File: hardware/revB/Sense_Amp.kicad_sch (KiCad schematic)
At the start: 3 parts, among them U17 INA240A3EDRQ1

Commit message: working revB
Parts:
- renumbered C52 to C36, C53 to C37, U17 to U15
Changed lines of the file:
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@@
   (symbol (lib_id "Device:C") (at 121.92 71.12 0) (unit 1)
     (in_bom yes) (on_board yes) (dnp no) (fields_autoplaced)
-    (property "Reference" "C52" (at 124.841 70.2115 0)
+    (property "Reference" "C36" (at 124.841 70.2115 0)
       (effects (font (size 1.27 1.27)) (justify left))
     )
@@
       (project "FP Interface Card"
         (path "/dc2801a1-d539-4721-b31f-fe196b9f13df/66fbc293-b490-4097-aa2e-a081509eef04/b12d78bf-aa15-467a-b4b1-b3adfb073398"
-          (reference "C52") (unit 1)
+          (reference "C36") (unit 1)
         )
         (path "/dc2801a1-d539-4721-b31f-fe196b9f13df/66fbc293-b490-4097-aa2e-a081509eef04/c0544bb0-133b-49a1-b8f9-e77504492c11"
-          (reference "C54") (unit 1)
+          (reference "C38") (unit 1)
         )
         (path "/dc2801a1-d539-4721-b31f-fe196b9f13df/66fbc293-b490-4097-aa2e-a081509eef04/055667d1-a090-4d44-b096-566c0357f041"
-          (reference "C59") (unit 1)
+          (reference "C41") (unit 1)
         )
       )
@@
   (symbol (lib_id "power:GND") (at 144.78 109.22 0) (unit 1)
     (in_bom yes) (on_board yes) (dnp no) (fields_autoplaced)
-    (property "Reference" "#PWR049" (at 144.78 115.57 0)
+    (property "Reference" "#PWR079" (at 144.78 115.57 0)
       (effects (font (size 1.27 1.27)) hide)
     )
@@
       (project "FP Interface Card"
         (path "/dc2801a1-d539-4721-b31f-fe196b9f13df/66fbc293-b490-4097-aa2e-a081509eef04/b12d78bf-aa15-467a-b4b1-b3adfb073398"
-          (reference "#PWR049") (unit 1)
+          (reference "#PWR079") (unit 1)
         )
         (path "/dc2801a1-d539-4721-b31f-fe196b9f13df/66fbc293-b490-4097-aa2e-a081509eef04/c0544bb0-133b-49a1-b8f9-e77504492c11"
-          (reference "#PWR051") (unit 1)
+          (reference "#PWR081") (unit 1)
         )
         (path "/dc2801a1-d539-4721-b31f-fe196b9f13df/66fbc293-b490-4097-aa2e-a081509eef04/055667d1-a090-4d44-b096-566c0357f041"
-          (reference "#PWR058") (unit 1)
+          (reference "#PWR087") (unit 1)
         )
       )
@@
   (symbol (lib_id "Device:C") (at 130.81 71.12 0) (unit 1)
     (in_bom yes) (on_board yes) (dnp no) (fields_autoplaced)
-    (property "Reference" "C53" (at 133.731 70.2115 0)
+    (property "Reference" "C37" (at 133.731 70.2115 0)
       (effects (font (size 1.27 1.27)) (justify left))
     )
@@
       (project "FP Interface Card"
         (path "/dc2801a1-d539-4721-b31f-fe196b9f13df/66fbc293-b490-4097-aa2e-a081509eef04/b12d78bf-aa15-467a-b4b1-b3adfb073398"
-          (reference "C53") (unit 1)
+          (reference "C37") (unit 1)
         )
         (path "/dc2801a1-d539-4721-b31f-fe196b9f13df/66fbc293-b490-4097-aa2e-a081509eef04/c0544bb0-133b-49a1-b8f9-e77504492c11"
-          (reference "C55") (unit 1)
+          (reference "C39") (unit 1)
         )
         (path "/dc2801a1-d539-4721-b31f-fe196b9f13df/66fbc293-b490-4097-aa2e-a081509eef04/055667d1-a090-4d44-b096-566c0357f041"
-          (reference "C60") (unit 1)
+          (reference "C42") (unit 1)
         )
       )
@@
   (symbol (lib_id "FP-Interface-Card:INA240AxxD") (at 147.32 97.79 0) (unit 1)
     (in_bom yes) (on_board yes) (dnp no)
-    (property "Reference" "U17" (at 152.4 91.44 0)
+    (property "Reference" "U15" (at 152.4 91.44 0)
       (effects (font (size 1.27 1.27)))
     )
@@
       (project "FP Interface Card"
         (path "/dc2801a1-d539-4721-b31f-fe196b9f13df/66fbc293-b490-4097-aa2e-a081509eef04/b12d78bf-aa15-467a-b4b1-b3adfb073398"
-          (reference "U17") (unit 1)
+          (reference "U15") (unit 1)
         )
         (path "/dc2801a1-d539-4721-b31f-fe196b9f13df/66fbc293-b490-4097-aa2e-a081509eef04/c0544bb0-133b-49a1-b8f9-e77504492c11"
-          (reference "U18") (unit 1)
+          (reference "U16") (unit 1)
         )
         (path "/dc2801a1-d539-4721-b31f-fe196b9f13df/66fbc293-b490-4097-aa2e-a081509eef04/055667d1-a090-4d44-b096-566c0357f041"
-          (reference "U20") (unit 1)
+          (reference "U18") (unit 1)
         )
       )
@@
   (symbol (lib_id "power:GND") (at 121.92 76.2 0) (unit 1)
     (in_bom yes) (on_board yes) (dnp no) (fields_autoplaced)
-    (property "Reference" "#PWR048" (at 121.92 82.55 0)
+    (property "Reference" "#PWR078" (at 121.92 82.55 0)
       (effects (font (size 1.27 1.27)) hide)
     )
@@
       (project "FP Interface Card"
         (path "/dc2801a1-d539-4721-b31f-fe196b9f13df/66fbc293-b490-4097-aa2e-a081509eef04/b12d78bf-aa15-467a-b4b1-b3adfb073398"
-          (reference "#PWR048") (unit 1)
+          (reference "#PWR078") (unit 1)
         )
         (path "/dc2801a1-d539-4721-b31f-fe196b9f13df/66fbc293-b490-4097-aa2e-a081509eef04/c0544bb0-133b-49a1-b8f9-e77504492c11"
-          (reference "#PWR050") (unit 1)
+          (reference "#PWR080") (unit 1)
         )
         (path "/dc2801a1-d539-4721-b31f-fe196b9f13df/66fbc293-b490-4097-aa2e-a081509eef04/055667d1-a090-4d44-b096-566c0357f041"
-          (reference "#PWR057") (unit 1)
+          (reference "#PWR086") (unit 1)
         )
       )

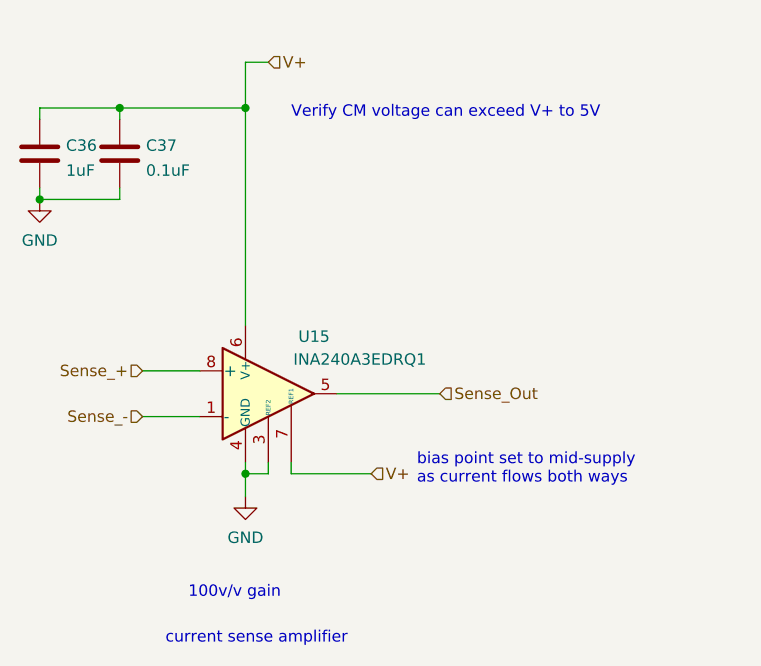
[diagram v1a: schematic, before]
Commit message: updated bp pinout, added payload current sensor
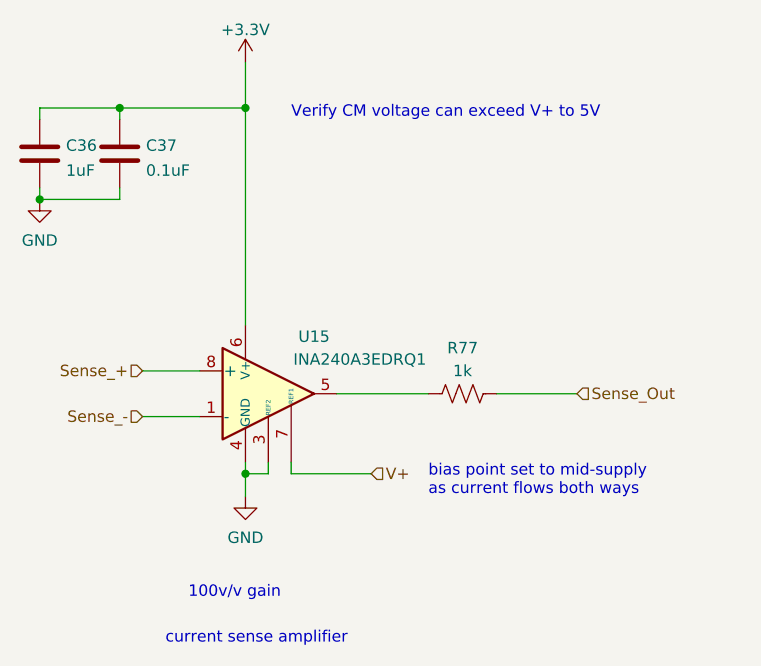
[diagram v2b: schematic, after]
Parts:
- added R77: 1k, Resistor_SMD:R_0603_1608Metric, symbol Device:R_US
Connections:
- net Sense_Out: now also R77.2; no longer U15.5
- net V+: no longer C36.1, C37.1, U15.6 (V+)
- new net: R77.1, U15.5
- new net +3V3: C36.1, C37.1, U15.6 (V+)
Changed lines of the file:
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@@
-    (stroke (width 0) (type default))
-  )
-  (wire (pts (xy 147.32 60.96) (xy 144.78 60.96))
     (stroke (width 0) (type default))
   )
@@
     (stroke (width 0) (type default))
   )
+  (wire (pts (xy 181.61 97.79) (xy 172.72 97.79))
+    (stroke (width 0) (type default))
+  )
   (wire (pts (xy 121.92 76.2) (xy 130.81 76.2))
     (stroke (width 0) (type default))
   )
-  (wire (pts (xy 154.94 97.79) (xy 166.37 97.79))
+  (wire (pts (xy 154.94 97.79) (xy 165.1 97.79))
     (stroke (width 0) (type default))
   )
@@
   )
   (text "bias point set to mid-supply\nas current flows both ways"
-    (at 163.83 107.95 0)
+    (at 165.1 109.22 0)
     (effects (font (size 1.27 1.27)) (justify left bottom))
   )
@@
     (effects (font (size 1.27 1.27)) (justify left))
   )
-  (hierarchical_label "V+" (shape input) (at 147.32 60.96 0) (fields_autoplaced)
-    (effects (font (size 1.27 1.27)) (justify left))
-  )
   (hierarchical_label "Sense_-" (shape input) (at 133.35 100.33 180) (fields_autoplaced)
     (effects (font (size 1.27 1.27)) (justify right))
   )
-  (hierarchical_label "Sense_Out" (shape input) (at 166.37 97.79 0) (fields_autoplaced)
+  (hierarchical_label "Sense_Out" (shape input) (at 181.61 97.79 0) (fields_autoplaced)
     (effects (font (size 1.27 1.27)) (justify left))
   )
@@
     )
   )
+  (symbol (lib_id "power:+3.3V") (at 144.78 60.96 0) (unit 1)
+    (in_bom yes) (on_board yes) (dnp no) (fields_autoplaced)
+    (property "Reference" "#PWR065" (at 144.78 64.77 0)
+      (effects (font (size 1.27 1.27)) hide)
+    )
+    (property "Value" "+3.3V" (at 144.78 57.3555 0)
+      (effects (font (size 1.27 1.27)))
+    )
+    (property "Footprint" "" (at 144.78 60.96 0)
+      (effects (font (size 1.27 1.27)) hide)
+    )
+    (property "Datasheet" "" (at 144.78 60.96 0)
+      (effects (font (size 1.27 1.27)) hide)
+    )
+    (pin "1")
+    (instances
+      (project "FP Interface Card"
+        (path "/dc2801a1-d539-4721-b31f-fe196b9f13df/66fbc293-b490-4097-aa2e-a081509eef04"
+          (reference "#PWR065") (unit 1)
+        )
+        (path "/dc2801a1-d539-4721-b31f-fe196b9f13df/66fbc293-b490-4097-aa2e-a081509eef04/b12d78bf-aa15-467a-b4b1-b3adfb073398"
+          (reference "#PWR038") (unit 1)
+        )
+        (path "/dc2801a1-d539-4721-b31f-fe196b9f13df/66fbc293-b490-4097-aa2e-a081509eef04/c0544bb0-133b-49a1-b8f9-e77504492c11"
+          (reference "#PWR0114") (unit 1)
+        )
+        (path "/dc2801a1-d539-4721-b31f-fe196b9f13df/66fbc293-b490-4097-aa2e-a081509eef04/055667d1-a090-4d44-b096-566c0357f041"
+          (reference "#PWR0115") (unit 1)
+        )
+      )
+    )
+  )
   (symbol (lib_id "power:GND") (at 144.78 109.22 0) (unit 1)
     (in_bom yes) (on_board yes) (dnp no) (fields_autoplaced)
@@
         )
       )
+    )
+  )
+  (symbol (lib_id "Device:R_US") (at 168.91 97.79 90) (unit 1)
+    (in_bom yes) (on_board yes) (dnp no) (fields_autoplaced)
+    (property "Reference" "R77" (at 168.91 92.71 90)
+      (effects (font (size 1.27 1.27)))
+    )
+    (property "Value" "1k" (at 168.91 95.25 90)
+      (effects (font (size 1.27 1.27)))
+    )
+    (property "Footprint" "Resistor_SMD:R_0603_1608Metric" (at 169.164 96.774 90)
+      (effects (font (size 1.27 1.27)) hide)
+    )
+    (property "Datasheet" "~" (at 168.91 97.79 0)
+      (effects (font (size 1.27 1.27)) hide)
+    )
+    (pin "1")
+    (pin "2")
+    (instances
+      (project "FP Interface Card"
+        (path "/dc2801a1-d539-4721-b31f-fe196b9f13df/66fbc293-b490-4097-aa2e-a081509eef04/c3b42a4a-1ed4-4106-b1d3-48a0726c5c74"
+          (reference "R77") (unit 1)
+        )
+        (path "/dc2801a1-d539-4721-b31f-fe196b9f13df/66fbc293-b490-4097-aa2e-a081509eef04/0d41b933-8bc8-4fa4-b49a-44e034cc3fe8"
+          (reference "R76") (unit 1)
+        )
+        (path "/dc2801a1-d539-4721-b31f-fe196b9f13df/66fbc293-b490-4097-aa2e-a081509eef04/3274ec9e-d72c-43b3-8471-ed8a89a9c8d1"
+          (reference "R78") (unit 1)
+        )
+        (path "/dc2801a1-d539-4721-b31f-fe196b9f13df/66fbc293-b490-4097-aa2e-a081509eef04/b12d78bf-aa15-467a-b4b1-b3adfb073398"
+          (reference "R23") (unit 1)
+        )
+        (path "/dc2801a1-d539-4721-b31f-fe196b9f13df/66fbc293-b490-4097-aa2e-a081509eef04/c0544bb0-133b-49a1-b8f9-e77504492c11"
+          (reference "R25") (unit 1)
+        )
+        (path "/dc2801a1-d539-4721-b31f-fe196b9f13df/66fbc293-b490-4097-aa2e-a081509eef04/055667d1-a090-4d44-b096-566c0357f041"
+          (reference "R26") (unit 1)
+        )
+      )

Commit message: updated files
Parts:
- renumbered C36 to C34, C37 to C35, U15 to U13
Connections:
- net +3V3 renamed +3.3V
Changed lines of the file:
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@@
   (paper "A4")
   (title_block
+    (rev "B")
     (company "Sierra Lobo INC")
   )
@@
   (symbol (lib_id "Device:C") (at 121.92 71.12 0) (unit 1)
     (in_bom yes) (on_board yes) (dnp no) (fields_autoplaced)
-    (property "Reference" "C36" (at 124.841 70.2115 0)
+    (property "Reference" "C34" (at 124.841 70.2115 0)
       (effects (font (size 1.27 1.27)) (justify left))
     )
@@
     (pin "2")
     (instances
-      (project "FP Interface Card"
-        (path "/dc2801a1-d539-4721-b31f-fe196b9f13df/66fbc293-b490-4097-aa2e-a081509eef04/b12d78bf-aa15-467a-b4b1-b3adfb073398"
+      (project "payload-interface-board"
+        (path "/dc2801a1-d539-4721-b31f-fe196b9f13df/66fbc293-b490-4097-aa2e-a081509eef04/b12d78bf-aa15-467a-b4b1-b3adfb073398"
+          (reference "C34") (unit 1)
+        )
+        (path "/dc2801a1-d539-4721-b31f-fe196b9f13df/66fbc293-b490-4097-aa2e-a081509eef04/c0544bb0-133b-49a1-b8f9-e77504492c11"
           (reference "C36") (unit 1)
         )
-        (path "/dc2801a1-d539-4721-b31f-fe196b9f13df/66fbc293-b490-4097-aa2e-a081509eef04/c0544bb0-133b-49a1-b8f9-e77504492c11"
-          (reference "C38") (unit 1)
-        )
-        (path "/dc2801a1-d539-4721-b31f-fe196b9f13df/66fbc293-b490-4097-aa2e-a081509eef04/055667d1-a090-4d44-b096-566c0357f041"
-          (reference "C41") (unit 1)
+        (path "/dc2801a1-d539-4721-b31f-fe196b9f13df/66fbc293-b490-4097-aa2e-a081509eef04/055667d1-a090-4d44-b096-566c0357f041"
+          (reference "C39") (unit 1)
         )
       )
@@
     (pin "1")
     (instances
-      (project "FP Interface Card"
+      (project "payload-interface-board"
         (path "/dc2801a1-d539-4721-b31f-fe196b9f13df/66fbc293-b490-4097-aa2e-a081509eef04"
           (reference "#PWR065") (unit 1)
         )
         (path "/dc2801a1-d539-4721-b31f-fe196b9f13df/66fbc293-b490-4097-aa2e-a081509eef04/b12d78bf-aa15-467a-b4b1-b3adfb073398"
-          (reference "#PWR038") (unit 1)
-        )
-        (path "/dc2801a1-d539-4721-b31f-fe196b9f13df/66fbc293-b490-4097-aa2e-a081509eef04/c0544bb0-133b-49a1-b8f9-e77504492c11"
-          (reference "#PWR0114") (unit 1)
-        )
-        (path "/dc2801a1-d539-4721-b31f-fe196b9f13df/66fbc293-b490-4097-aa2e-a081509eef04/055667d1-a090-4d44-b096-566c0357f041"
-          (reference "#PWR0115") (unit 1)
+          (reference "#PWR071") (unit 1)
+        )
+        (path "/dc2801a1-d539-4721-b31f-fe196b9f13df/66fbc293-b490-4097-aa2e-a081509eef04/c0544bb0-133b-49a1-b8f9-e77504492c11"
+          (reference "#PWR074") (unit 1)
+        )
+        (path "/dc2801a1-d539-4721-b31f-fe196b9f13df/66fbc293-b490-4097-aa2e-a081509eef04/055667d1-a090-4d44-b096-566c0357f041"
+          (reference "#PWR081") (unit 1)
         )
       )
@@
   (symbol (lib_id "power:GND") (at 144.78 109.22 0) (unit 1)
     (in_bom yes) (on_board yes) (dnp no) (fields_autoplaced)
-    (property "Reference" "#PWR079" (at 144.78 115.57 0)
+    (property "Reference" "#PWR073" (at 144.78 115.57 0)
       (effects (font (size 1.27 1.27)) hide)
     )
@@
     (pin "1")
     (instances
-      (project "FP Interface Card"
-        (path "/dc2801a1-d539-4721-b31f-fe196b9f13df/66fbc293-b490-4097-aa2e-a081509eef04/b12d78bf-aa15-467a-b4b1-b3adfb073398"
-          (reference "#PWR079") (unit 1)
-        )
-        (path "/dc2801a1-d539-4721-b31f-fe196b9f13df/66fbc293-b490-4097-aa2e-a081509eef04/c0544bb0-133b-49a1-b8f9-e77504492c11"
-          (reference "#PWR081") (unit 1)
-        )
-        (path "/dc2801a1-d539-4721-b31f-fe196b9f13df/66fbc293-b490-4097-aa2e-a081509eef04/055667d1-a090-4d44-b096-566c0357f041"
-          (reference "#PWR087") (unit 1)
+      (project "payload-interface-board"
+        (path "/dc2801a1-d539-4721-b31f-fe196b9f13df/66fbc293-b490-4097-aa2e-a081509eef04/b12d78bf-aa15-467a-b4b1-b3adfb073398"
+          (reference "#PWR073") (unit 1)
+        )
+        (path "/dc2801a1-d539-4721-b31f-fe196b9f13df/66fbc293-b490-4097-aa2e-a081509eef04/c0544bb0-133b-49a1-b8f9-e77504492c11"
+          (reference "#PWR076") (unit 1)
+        )
+        (path "/dc2801a1-d539-4721-b31f-fe196b9f13df/66fbc293-b490-4097-aa2e-a081509eef04/055667d1-a090-4d44-b096-566c0357f041"
+          (reference "#PWR083") (unit 1)
         )
       )
@@
     (pin "2")
     (instances
-      (project "FP Interface Card"
+      (project "payload-interface-board"
         (path "/dc2801a1-d539-4721-b31f-fe196b9f13df/66fbc293-b490-4097-aa2e-a081509eef04/c3b42a4a-1ed4-4106-b1d3-48a0726c5c74"
           (reference "R77") (unit 1)
@@
         )
         (path "/dc2801a1-d539-4721-b31f-fe196b9f13df/66fbc293-b490-4097-aa2e-a081509eef04/b12d78bf-aa15-467a-b4b1-b3adfb073398"
-          (reference "R23") (unit 1)
-        )
-        (path "/dc2801a1-d539-4721-b31f-fe196b9f13df/66fbc293-b490-4097-aa2e-a081509eef04/c0544bb0-133b-49a1-b8f9-e77504492c11"
-          (reference "R25") (unit 1)
-        )
-        (path "/dc2801a1-d539-4721-b31f-fe196b9f13df/66fbc293-b490-4097-aa2e-a081509eef04/055667d1-a090-4d44-b096-566c0357f041"
-          (reference "R26") (unit 1)
+          (reference "R48") (unit 1)
+        )
+        (path "/dc2801a1-d539-4721-b31f-fe196b9f13df/66fbc293-b490-4097-aa2e-a081509eef04/c0544bb0-133b-49a1-b8f9-e77504492c11"
+          (reference "R49") (unit 1)
+        )
+        (path "/dc2801a1-d539-4721-b31f-fe196b9f13df/66fbc293-b490-4097-aa2e-a081509eef04/055667d1-a090-4d44-b096-566c0357f041"
+          (reference "R51") (unit 1)
         )
       )
@@
   (symbol (lib_id "Device:C") (at 130.81 71.12 0) (unit 1)
     (in_bom yes) (on_board yes) (dnp no) (fields_autoplaced)
-    (property "Reference" "C37" (at 133.731 70.2115 0)
+    (property "Reference" "C35" (at 133.731 70.2115 0)
       (effects (font (size 1.27 1.27)) (justify left))
     )
@@
     (pin "2")
     (instances
-      (project "FP Interface Card"
-        (path "/dc2801a1-d539-4721-b31f-fe196b9f13df/66fbc293-b490-4097-aa2e-a081509eef04/b12d78bf-aa15-467a-b4b1-b3adfb073398"
+      (project "payload-interface-board"
+        (path "/dc2801a1-d539-4721-b31f-fe196b9f13df/66fbc293-b490-4097-aa2e-a081509eef04/b12d78bf-aa15-467a-b4b1-b3adfb073398"
+          (reference "C35") (unit 1)
+        )
+        (path "/dc2801a1-d539-4721-b31f-fe196b9f13df/66fbc293-b490-4097-aa2e-a081509eef04/c0544bb0-133b-49a1-b8f9-e77504492c11"
           (reference "C37") (unit 1)
         )
-        (path "/dc2801a1-d539-4721-b31f-fe196b9f13df/66fbc293-b490-4097-aa2e-a081509eef04/c0544bb0-133b-49a1-b8f9-e77504492c11"
-          (reference "C39") (unit 1)
-        )
-        (path "/dc2801a1-d539-4721-b31f-fe196b9f13df/66fbc293-b490-4097-aa2e-a081509eef04/055667d1-a090-4d44-b096-566c0357f041"
-          (reference "C42") (unit 1)
+        (path "/dc2801a1-d539-4721-b31f-fe196b9f13df/66fbc293-b490-4097-aa2e-a081509eef04/055667d1-a090-4d44-b096-566c0357f041"
+          (reference "C40") (unit 1)
         )
       )
@@
   (symbol (lib_id "FP-Interface-Card:INA240AxxD") (at 147.32 97.79 0) (unit 1)
     (in_bom yes) (on_board yes) (dnp no)
-    (property "Reference" "U15" (at 152.4 91.44 0)
+    (property "Reference" "U13" (at 152.4 91.44 0)
       (effects (font (size 1.27 1.27)))
     )
@@
     (pin "8")
     (instances
-      (project "FP Interface Card"
-        (path "/dc2801a1-d539-4721-b31f-fe196b9f13df/66fbc293-b490-4097-aa2e-a081509eef04/b12d78bf-aa15-467a-b4b1-b3adfb073398"
-          (reference "U15") (unit 1)
-        )
-        (path "/dc2801a1-d539-4721-b31f-fe196b9f13df/66fbc293-b490-4097-aa2e-a081509eef04/c0544bb0-133b-49a1-b8f9-e77504492c11"
+      (project "payload-interface-board"
+        (path "/dc2801a1-d539-4721-b31f-fe196b9f13df/66fbc293-b490-4097-aa2e-a081509eef04/b12d78bf-aa15-467a-b4b1-b3adfb073398"
+          (reference "U13") (unit 1)
+        )
+        (path "/dc2801a1-d539-4721-b31f-fe196b9f13df/66fbc293-b490-4097-aa2e-a081509eef04/c0544bb0-133b-49a1-b8f9-e77504492c11"
+          (reference "U14") (unit 1)
+        )
+        (path "/dc2801a1-d539-4721-b31f-fe196b9f13df/66fbc293-b490-4097-aa2e-a081509eef04/055667d1-a090-4d44-b096-566c0357f041"
           (reference "U16") (unit 1)
         )
-        (path "/dc2801a1-d539-4721-b31f-fe196b9f13df/66fbc293-b490-4097-aa2e-a081509eef04/055667d1-a090-4d44-b096-566c0357f041"
-          (reference "U18") (unit 1)
-        )
       )
     )
@@
   (symbol (lib_id "power:GND") (at 121.92 76.2 0) (unit 1)
     (in_bom yes) (on_board yes) (dnp no) (fields_autoplaced)
-    (property "Reference" "#PWR078" (at 121.92 82.55 0)
+    (property "Reference" "#PWR072" (at 121.92 82.55 0)
       (effects (font (size 1.27 1.27)) hide)
     )
@@
     (pin "1")
     (instances
-      (project "FP Interface Card"
-        (path "/dc2801a1-d539-4721-b31f-fe196b9f13df/66fbc293-b490-4097-aa2e-a081509eef04/b12d78bf-aa15-467a-b4b1-b3adfb073398"
-          (reference "#PWR078") (unit 1)
-        )
-        (path "/dc2801a1-d539-4721-b31f-fe196b9f13df/66fbc293-b490-4097-aa2e-a081509eef04/c0544bb0-133b-49a1-b8f9-e77504492c11"
-          (reference "#PWR080") (unit 1)
-        )
-        (path "/dc2801a1-d539-4721-b31f-fe196b9f13df/66fbc293-b490-4097-aa2e-a081509eef04/055667d1-a090-4d44-b096-566c0357f041"
-          (reference "#PWR086") (unit 1)
-        )
-      )
+      (project "payload-interface-board"
+        (path "/dc2801a1-d539-4721-b31f-fe196b9f13df/66fbc293-b490-4097-aa2e-a081509eef04/b12d78bf-aa15-467a-b4b1-b3adfb073398"
+          (reference "#PWR072") (unit 1)
+        )
+        (path "/dc2801a1-d539-4721-b31f-fe196b9f13df/66fbc293-b490-4097-aa2e-a081509eef04/c0544bb0-133b-49a1-b8f9-e77504492c11"
+          (reference "#PWR075") (unit 1)
+        )
+        (path "/dc2801a1-d539-4721-b31f-fe196b9f13df/66fbc293-b490-4097-aa2e-a081509eef04/055667d1-a090-4d44-b096-566c0357f041"
+          (reference "#PWR082") (unit 1)
+        )
+      )

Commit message: working
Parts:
- removed R77: 1k, Resistor_SMD:R_0603_1608Metric, symbol Device:R_US
- removed U13: INA240A3EDRQ1, Package_SO:SOIC-8_3.9x4.9mm_P1.27mm, symbol FP-Interface-Card:INA240AxxD
- added U13: INA199A2xDCK, Package_TO_SOT_SMD:SOT-363_SC-70-6, symbol Amplifier_Current:INA199xxDCK
- C37: renamed from C34; value 1uF -> 0.1uF
- C38: renamed from C35; value 0.1uF -> 0.01uF
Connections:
- net +3.3V: now also U13.3 (V+)
- net GND: now also U13.2 (GND)
- new net +: U13.4 (+)
- new net -: U13.5 (-)
- new net OUT: U13.6
- new net REF: U13.1 (REF)
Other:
- note removed: "Verify CM voltage can exceed V+ to 5V"
- company: Sierra Lobo INC -> (none)
- title: (none) -> Foras Promineo Payload Interface Board
- moved on the sheet: C37, C38
